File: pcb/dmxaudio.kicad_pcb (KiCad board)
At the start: 2 copper layers, 150 x 82 mm, 16 parts, among them J1 USB_A, J2 RJ45_Bel_SI-60062-F, J3 RJ45, SW1 SW_DIP_x09, SW2 SW_DPDT_x2, U1 Teensy4.1, U2 SN65HVD11HD

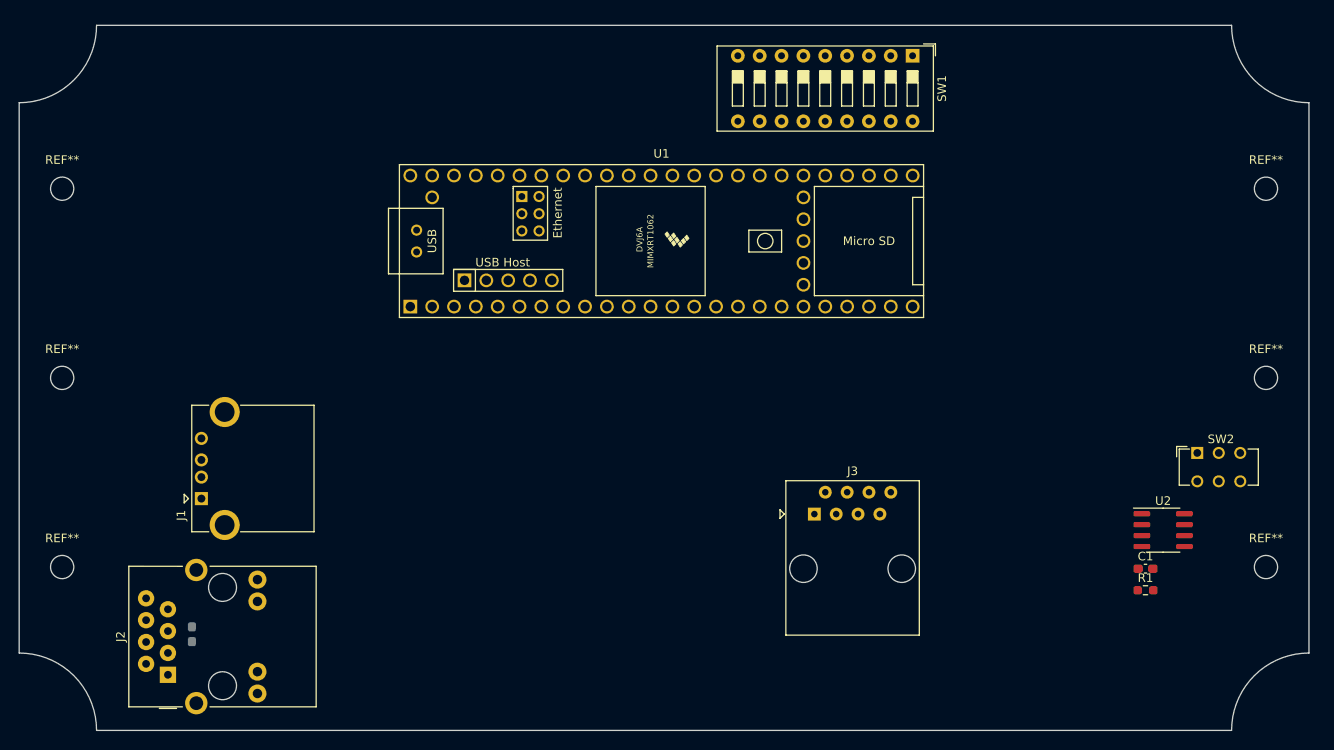
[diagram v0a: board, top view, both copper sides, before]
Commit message: Updating schematic based on review from Mike
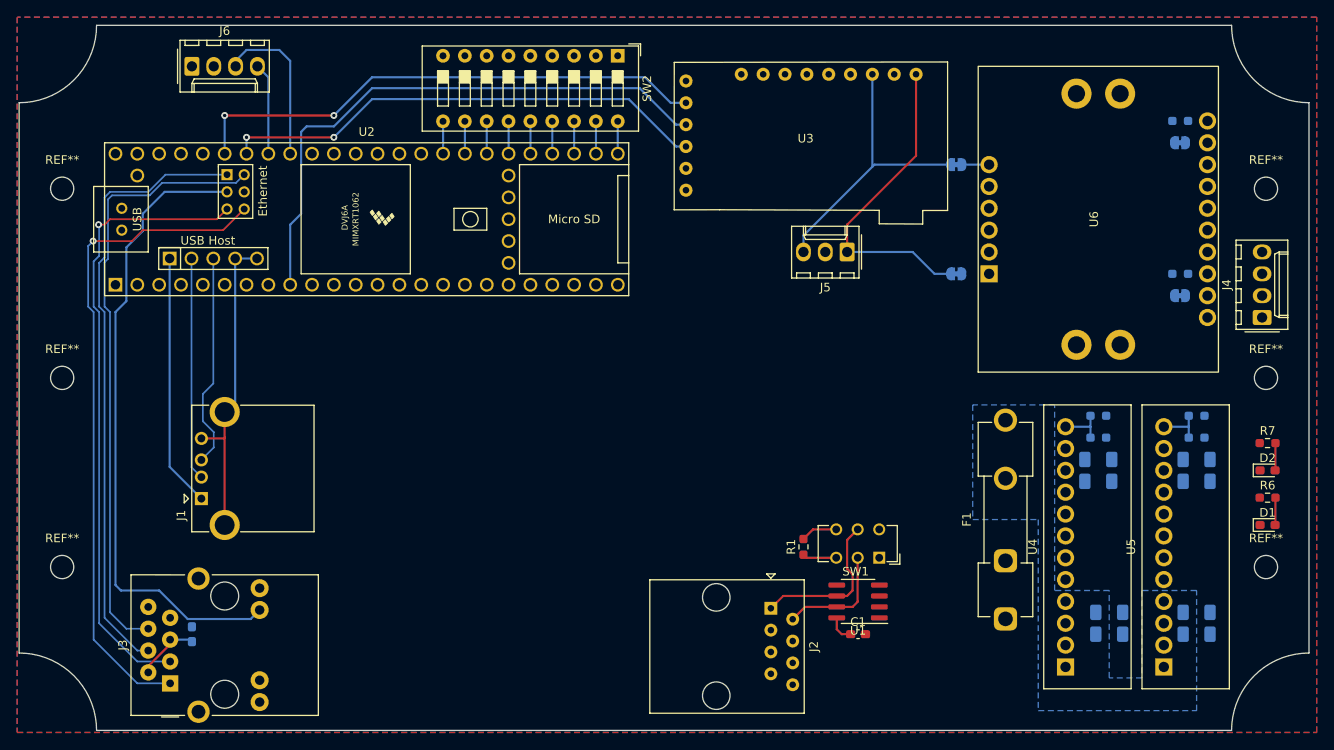
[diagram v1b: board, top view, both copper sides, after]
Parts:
- added C10: DNP, Capacitor_SMD:C_1206_3216Metric_Pad1.33x1.80mm_HandSolder, B.Cu at (201.9, 110.5)
- added C3: 10u, Capacitor_SMD:C_1206_3216Metric_Pad1.33x1.80mm_HandSolder, B.Cu at (191.8, 130.8)
- added C4: DNP, Capacitor_SMD:C_1206_3216Metric_Pad1.33x1.80mm_HandSolder, B.Cu at (191.8, 128.3)
- added C5: DNP, Capacitor_SMD:C_1206_3216Metric_Pad1.33x1.80mm_HandSolder, B.Cu at (201.9, 128.3)
- added C6: 10u, Capacitor_SMD:C_1206_3216Metric_Pad1.33x1.80mm_HandSolder, B.Cu at (201.9, 130.8)
- added C7: 22u, Capacitor_SMD:C_1206_3216Metric_Pad1.33x1.80mm_HandSolder, B.Cu at (190.5, 113.0)
- added C8: DNP, Capacitor_SMD:C_1206_3216Metric_Pad1.33x1.80mm_HandSolder, B.Cu at (190.5, 110.5)
- added C9: 22u, Capacitor_SMD:C_1206_3216Metric_Pad1.33x1.80mm_HandSolder, B.Cu at (201.9, 113.0)
- added D1: LED, LED_SMD:LED_0603_1608Metric_Pad1.05x0.95mm_HandSolder, F.Cu at (210.2, 118.1)
- added D2: LED, LED_SMD:LED_0603_1608Metric_Pad1.05x0.95mm_HandSolder, F.Cu at (210.2, 111.8)
- added F1: Fuse, Fuse:Fuseholder_Clip-5x20mm_Keystone_3517_Inline_P23.11x6.76mm_D1.70mm_Horizontal, F.Cu at (179.7, 129.0)
- added J4: Conn_01x04, Connector_Molex:Molex_KK-254_AE-6410-04A_1x04_P2.54mm_Vertical, F.Cu at (209.6, 94.0)
- added J5: Conn_01x03, Connector_Molex:Molex_KK-254_AE-6410-03A_1x03_P2.54mm_Vertical, F.Cu at (161.3, 86.4)
- added J6: Conn_01x04, Connector_Molex:Molex_KK-254_AE-6410-04A_1x04_P2.54mm_Vertical, F.Cu at (85.1, 64.8)
- added JP1: SolderJumper_2_Bridged, Jumper:SolderJumper-2_P1.3mm_Bridged_RoundedPad1.0x1.5mm, B.Cu at (174.0, 88.9)
- added JP2: SolderJumper_2_Bridged, Jumper:SolderJumper-2_P1.3mm_Bridged_RoundedPad1.0x1.5mm, B.Cu at (174.0, 76.2)
- added JP3: SolderJumper_2_Bridged, Jumper:SolderJumper-2_P1.3mm_Bridged_RoundedPad1.0x1.5mm, B.Cu at (200.0, 73.7)
- added JP4: SolderJumper_2_Bridged, Jumper:SolderJumper-2_P1.3mm_Bridged_RoundedPad1.0x1.5mm, B.Cu at (200.0, 91.4)
- added R2: DNP, Resistor_SMD:R_0603_1608Metric_Pad0.98x0.95mm_HandSolder, B.Cu at (190.5, 105.4)
- added R3: DNP, Resistor_SMD:R_0603_1608Metric_Pad0.98x0.95mm_HandSolder, B.Cu at (190.5, 108.0)
- added R4: DNP, Resistor_SMD:R_0603_1608Metric_Pad0.98x0.95mm_HandSolder, B.Cu at (201.9, 105.4)
- added R5: DNP, Resistor_SMD:R_0603_1608Metric_Pad0.98x0.95mm_HandSolder, B.Cu at (201.9, 108.0)
- added R6: 1K, Resistor_SMD:R_0603_1608Metric_Pad0.98x0.95mm_HandSolder, F.Cu at (210.2, 114.9)
- added R7: 2.7K, Resistor_SMD:R_0603_1608Metric_Pad0.98x0.95mm_HandSolder, F.Cu at (210.2, 108.6)
- added R8: DNP, Resistor_SMD:R_0603_1608Metric_Pad0.98x0.95mm_HandSolder, B.Cu at (200.0, 71.1)
- added R9: DNP, Resistor_SMD:R_0603_1608Metric_Pad0.98x0.95mm_HandSolder, B.Cu at (200.0, 88.9)
- added U3: ~, dmxaudio:GY-PCM5102, F.Cu at (157.5, 73.7)
- added U4: K78L05-3AR3, dmxaudio:K78LXX-3AR3, F.Cu at (186.7, 120.7)
- added U5: K78L12-3AR3, dmxaudio:K78LXX-3AR3, F.Cu at (198.1, 120.7)
- added U6: CJMCU-8006, dmxaudio:CJMCU-8006, F.Cu at (190.5, 82.5)
- J2: value RJ45_Bel_SI-60062-F -> RJ45; footprint Connector_RJ:RJ45_Bel_SI-60062-F -> Connector_RJ:RJ45_Amphenol_54602-x08_Horizontal
- J3: value RJ45 -> RJ45_Bel_SI-60062-F; footprint Connector_RJ:RJ45_Amphenol_54602-x08_Horizontal -> Connector_RJ:RJ45_Bel_SI-60062-F
- SW1: value SW_DIP_x09 -> SW_DPDT_x2; footprint Button_Switch_THT:SW_DIP_SPSTx09_Slide_9.78x25.04mm_W7.62mm_P2.54mm -> Button_Switch_THT:SW_CuK_JS202011CQN_DPDT_Straight
- SW2: value SW_DPDT_x2 -> SW_DIP_x09; footprint Button_Switch_THT:SW_CuK_JS202011CQN_DPDT_Straight -> Button_Switch_THT:SW_DIP_SPSTx09_Slide_9.78x25.04mm_W7.62mm_P2.54mm
- U1: value Teensy4.1 -> SN65HVD11HD; footprint teensy:Teensy41 -> Package_SO:SOIC-8_3.9x4.9mm_P1.27mm
- U2: value SN65HVD11HD -> Teensy4.1; footprint Package_SO:SOIC-8_3.9x4.9mm_P1.27mm -> teensy:Teensy41
- moved U2 99.4 mm to (105.4, 82.5)
- moved SW2 81.7 mm to (134.6, 63.5), turned to -90 degrees
- moved J3 77.5 mm to (82.6, 136.5), turned to 90 degrees
- moved J2 70.5 mm to (152.4, 127.8), turned to -90 degrees
- moved SW1 58.5 mm to (165.0, 121.9), turned to 180 degrees
- moved U1 47.7 mm to (162.6, 127.0), turned to 180 degrees
- moved R1 40.1 mm to (156.2, 120.7), turned to 90 degrees
- moved C1 34.3 mm to (162.6, 130.8)
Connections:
- C2 pad 1: Net-(J2-RCT) -> Net-(J3-RCT)
- J1 pad 1: Net-(J1-VBUS) -> /MCU/USB_VBUS
- J1 pad 2: Net-(J1-D-) -> /MCU/USB_D-
- J1 pad 3: Net-(J1-D+) -> /MCU/USB_D+
- J1 pad 4: Net-(J1-GND) -> /MCU/USB_GND
- J1 pad 5: Net-(J1-GND) -> /MCU/USB_GND
- J2 pad 1: Net-(J2-TD+) -> /MCU/RS485_A
- J2 pad 2: Net-(J2-RCT) -> /MCU/RS485_B
- J2 pad 3: Net-(J2-TD-) -> unconnected-(J2-Pad3)
- J2 pad 4: Net-(J2-RD+) -> Net-(F1-Pad1)
- J2 pad 5: Net-(J2-RCT) -> Net-(F1-Pad1)
- J2 pad 6: Net-(J2-RD-) -> unconnected-(J2-Pad6)
- J2 pad 7: unconnected-(J2-NC-Pad7) -> GND
- J3 pad 1: unconnected-(J3-Pad1) -> /MCU/ETHERNET_T+
- J3 pad 2: unconnected-(J3-Pad2) -> Net-(J3-RCT)
- J3 pad 3: unconnected-(J3-Pad3) -> /MCU/ETHERNET_T-
- J3 pad 4: unconnected-(J3-Pad4) -> /MCU/ETHERNET_R+
- J3 pad 5: unconnected-(J3-Pad5) -> Net-(J3-RCT)
- J3 pad 6: unconnected-(J3-Pad6) -> /MCU/ETHERNET_R-
- J3 pad 8: unconnected-(J3-Pad8) -> GND
- R1 pad 1: Net-(SW2A-C) -> Net-(SW1A-C)
- R1 pad 2: Net-(SW2B-C) -> Net-(SW1B-C)
- SW1 pad 1: GND -> unconnected-(SW1A-A-Pad1)
- SW1 pad 2: GND -> /MCU/RS485_B
- SW1 pad 3: GND -> Net-(SW1A-C)
- SW1 pad 4: GND -> unconnected-(SW1B-A-Pad4)
- SW1 pad 5: GND -> /MCU/RS485_A
- SW1 pad 6: GND -> Net-(SW1B-C)
- SW2 pad 1: unconnected-(SW2A-A-Pad1) -> GND
- SW2 pad 2: /RS485_B -> GND
- SW2 pad 3: Net-(SW2A-C) -> GND
- SW2 pad 4: unconnected-(SW2B-A-Pad4) -> GND
- SW2 pad 5: /RS485_A -> GND
- SW2 pad 6: Net-(SW2B-C) -> GND
- U1 pad 1: GND -> /MCU/DMX_DATA
- U1 pad 2: unconnected-(U1-0_RX1_CRX2_CS1-Pad2) -> GND
- U1 pad 3: unconnected-(U1-1_TX1_CTX2_MISO1-Pad3) -> GND
- U1 pad 4: unconnected-(U1-2_OUT2-Pad4) -> GND
- U1 pad 5: unconnected-(U1-3_LRCLK2-Pad5) -> GND
- U1 pad 6: unconnected-(U1-4_BCLK2-Pad6) -> /MCU/RS485_A
- U1 pad 7: unconnected-(U1-5_IN2-Pad7) -> /MCU/RS485_B
- U1 pad 8: unconnected-(U1-6_OUT1D-Pad8) -> +3V3
- U2 pad 1: /DMX_DATA -> GND
- U2 pad 2: GND -> unconnected-(U2-0_RX1_CRX2_CS1-Pad2)
- U2 pad 3: GND -> unconnected-(U2-1_TX1_CTX2_MISO1-Pad3)
- U2 pad 4: GND -> unconnected-(U2-2_OUT2-Pad4)
- U2 pad 5: GND -> unconnected-(U2-3_LRCLK2-Pad5)
- U2 pad 6: /RS485_A -> unconnected-(U2-4_BCLK2-Pad6)
- U2 pad 7: /RS485_B -> unconnected-(U2-5_IN2-Pad7)
- U2 pad 8: +3V3 -> unconnected-(U2-6_OUT1D-Pad8)
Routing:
- net /MCU/ETHERNET_T+: track 0.00 -> 77.0 mm, vias 0 -> 1
- net /MCU/ETHERNET_LED: track 0.00 -> 74.2 mm
- net /MCU/ETHERNET_T-: track 0.00 -> 72.7 mm, vias 0 -> 1
- net /MCU/ETHERNET_R+: track 0.00 -> 71.4 mm
- net /MCU/ETHERNET_R-: track 0.00 -> 70.7 mm
- net /DAC/DATA: track 0.00 -> 66.9 mm
- net /DAC/BCLK: track 0.00 -> 61.2 mm, vias 0 -> 2
- net /DAC/LRCLK: track 0.00 -> 57.1 mm, vias 0 -> 2
- net /DAC/LEFT: track 0.00 -> 37.1 mm
- net /MCU/USB_GND: track 0.00 -> 36.8 mm
- net /DAC/RIGHT: track 0.00 -> 33.2 mm
- net /MCU/USB_VBUS: track 0.00 -> 29.4 mm
- net /MCU/USB_D-: track 0.00 -> 25.9 mm
- net /MCU/USB_D+: track 0.00 -> 25.0 mm
- net /MCU/SDA: track 0.00 -> 18.8 mm
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- added copper zone on B.Cu, net +24V
- added copper zone on B.Cu, net GND
- added copper zone on F.Cu, net GND

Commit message: Adding PCB files sent off to fab
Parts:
- added Brd1: SSD1306, dmxaudio:128x64OLED, F.Cu at (87.4, 108.1)
- added C11: 470u DNP, Capacitor_THT:CP_Radial_D8.0mm_P2.50mm, F.Cu at (210.1, 86.0)
- added C12: 22u DNP, Capacitor_SMD:C_1206_3216Metric_Pad1.33x1.80mm_HandSolder, B.Cu at (199.1, 78.7)
- added C13: 22u DNP, Capacitor_SMD:C_1206_3216Metric_Pad1.33x1.80mm_HandSolder, B.Cu at (199.4, 87.6)
- added C14: 22u DNP, Capacitor_SMD:C_1206_3216Metric_Pad1.33x1.80mm_HandSolder, B.Cu at (146.6, 79.2)
- added C15: 22u DNP, Capacitor_SMD:C_1206_3216Metric_Pad1.33x1.80mm_HandSolder, B.Cu at (111.8, 86.4)
- added C16: 10u DNP, Capacitor_SMD:C_1206_3216Metric_Pad1.33x1.80mm_HandSolder, F.Cu at (81.3, 70.5)
- added C17: 10u DNP, Capacitor_SMD:C_1206_3216Metric_Pad1.33x1.80mm_HandSolder, F.Cu at (173.5, 109.3)
- added C18: 10u DNP, Capacitor_SMD:C_1206_3216Metric_Pad1.33x1.80mm_HandSolder, F.Cu at (76.2, 70.5)
- added J7: Conn_01x06, Connector_Molex:Molex_KK-254_AE-6410-06A_1x06_P2.54mm_Vertical, F.Cu at (170.7, 137.7)
- added R10: 10K, Resistor_SMD:R_0603_1608Metric_Pad0.98x0.95mm_HandSolder, F.Cu at (167.4, 104.2)
- added SW3: SW_DPDT_x2, Button_Switch_THT:SW_CuK_JS202011CQN_DPDT_Straight, F.Cu at (67.9, 92.6)
- F1: footprint Fuse:Fuseholder_Clip-5x20mm_Keystone_3517_Inline_P23.11x6.76mm_D1.70mm_Horizontal -> dmxaudio:XF-506P
- moved J4 37.9 mm to (172.2, 100.3)
- moved C1 23.1 mm to (171.2, 109.4), turned to 90 degrees
- moved J2 18.5 mm to (169.6, 120.9)
- moved U1 18.3 mm to (167.4, 109.4), turned to -90 degrees
- moved SW1 15.3 mm to (162.3, 106.9), turned to -90 degrees
- moved F1 10.0 mm to (179.1, 119.0)
- moved R1 6.90 mm to (161.0, 115.7), turned to 180 degrees
- moved R9 5.08 mm to (200.0, 94.0)
- moved J1 4.23 mm to (90.4, 115.1)
- moved C2 3.05 mm to (88.1, 130.8)
- moved J3 3.05 mm to (85.6, 136.5)
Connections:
- net Net-(F1-Pad1) renamed /24V_PREFUSE
- U1 pad 2: GND -> /MCU/RDM_SEND
- U1 pad 3: GND -> /MCU/RDM_SEND
- U1 pad 4: GND -> /MCU/RDM_DATA
- U2 pad 21: unconnected-(U2-29_TX7-Pad21) -> /MCU/RDM_DATA
- U2 pad 22: unconnected-(U2-30_CRX3-Pad22) -> /MCU/RDM_SEND
- U2 pad 48: /Amplifier/5V -> Net-(SW3B-B)
- U3 pad 10: GND -> unconnected-(U3-FMT-Pad10)
- U3 pad 7: GND -> unconnected-(U3-FLT-Pad7)
- U3 pad 8: GND -> unconnected-(U3-DEMP-Pad8)
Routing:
- net /Amplifier/5V: track 0.00 -> 278.2 mm, vias 0 -> 4
- net +3V3: track 3.18 -> 157.6 mm, vias 0 -> 1
- net /MCU/MUTE: track 0.00 -> 124.1 mm, vias 0 -> 3
- net /MCU/~{SD}: track 0.00 -> 119.8 mm, vias 0 -> 5
- net /MCU/DMX_DATA: track 0.00 -> 57.3 mm
- net /MCU/RDM_SEND: track 0.00 -> 52.6 mm
- net /MCU/RDM_DATA: track 0.00 -> 50.5 mm
- net /Amplifier/SPEAKER_R+: track 0.00 -> 48.6 mm
- net /Amplifier/SPEAKER_R-: track 0.00 -> 39.6 mm
- net /MCU/RS485_B: track 13.5 -> 43.2 mm
- net /MCU/RS485_A: track 18.2 -> 43.8 mm
- net /MCU/SDA: track 18.8 -> 43.5 mm, vias 0 -> 2
- net /MCU/SCL: track 10.7 -> 35.4 mm, vias 0 -> 2
- net /Amplifier/SPEAKER_L+: track 0.00 -> 23.5 mm
- net /Amplifier/12V: track 0.00 -> 23.3 mm
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- added copper zone on F.Cu, net /24V_PREFUSE
- added copper zone on B.Cu, net /Amplifier/12V
- added copper zone on F.Cu, net /Amplifier/12V
- added copper zone on B.Cu, net /Amplifier/5V
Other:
- outline, holes or cut-outs redrawn
- board text added: "DMXAudio Revision 1 by rglenn 2023-10-09"
- board text added: "PO45"
- board text added: "USB"
